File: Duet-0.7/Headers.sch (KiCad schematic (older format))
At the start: 12 parts, among them J1 EXPANSION, J10 E0 MOT/STOP, J11 E0 HEAT/TEMP/FAN, J20 5V_PS, J23 POWER IN, J24 GND V_IN, J28 Probe, J4 BED HEATER, J5 BED TEMP, J7 Z MOT/STOP, J8 Y MOT/STOP, J9 X MOT/STOP

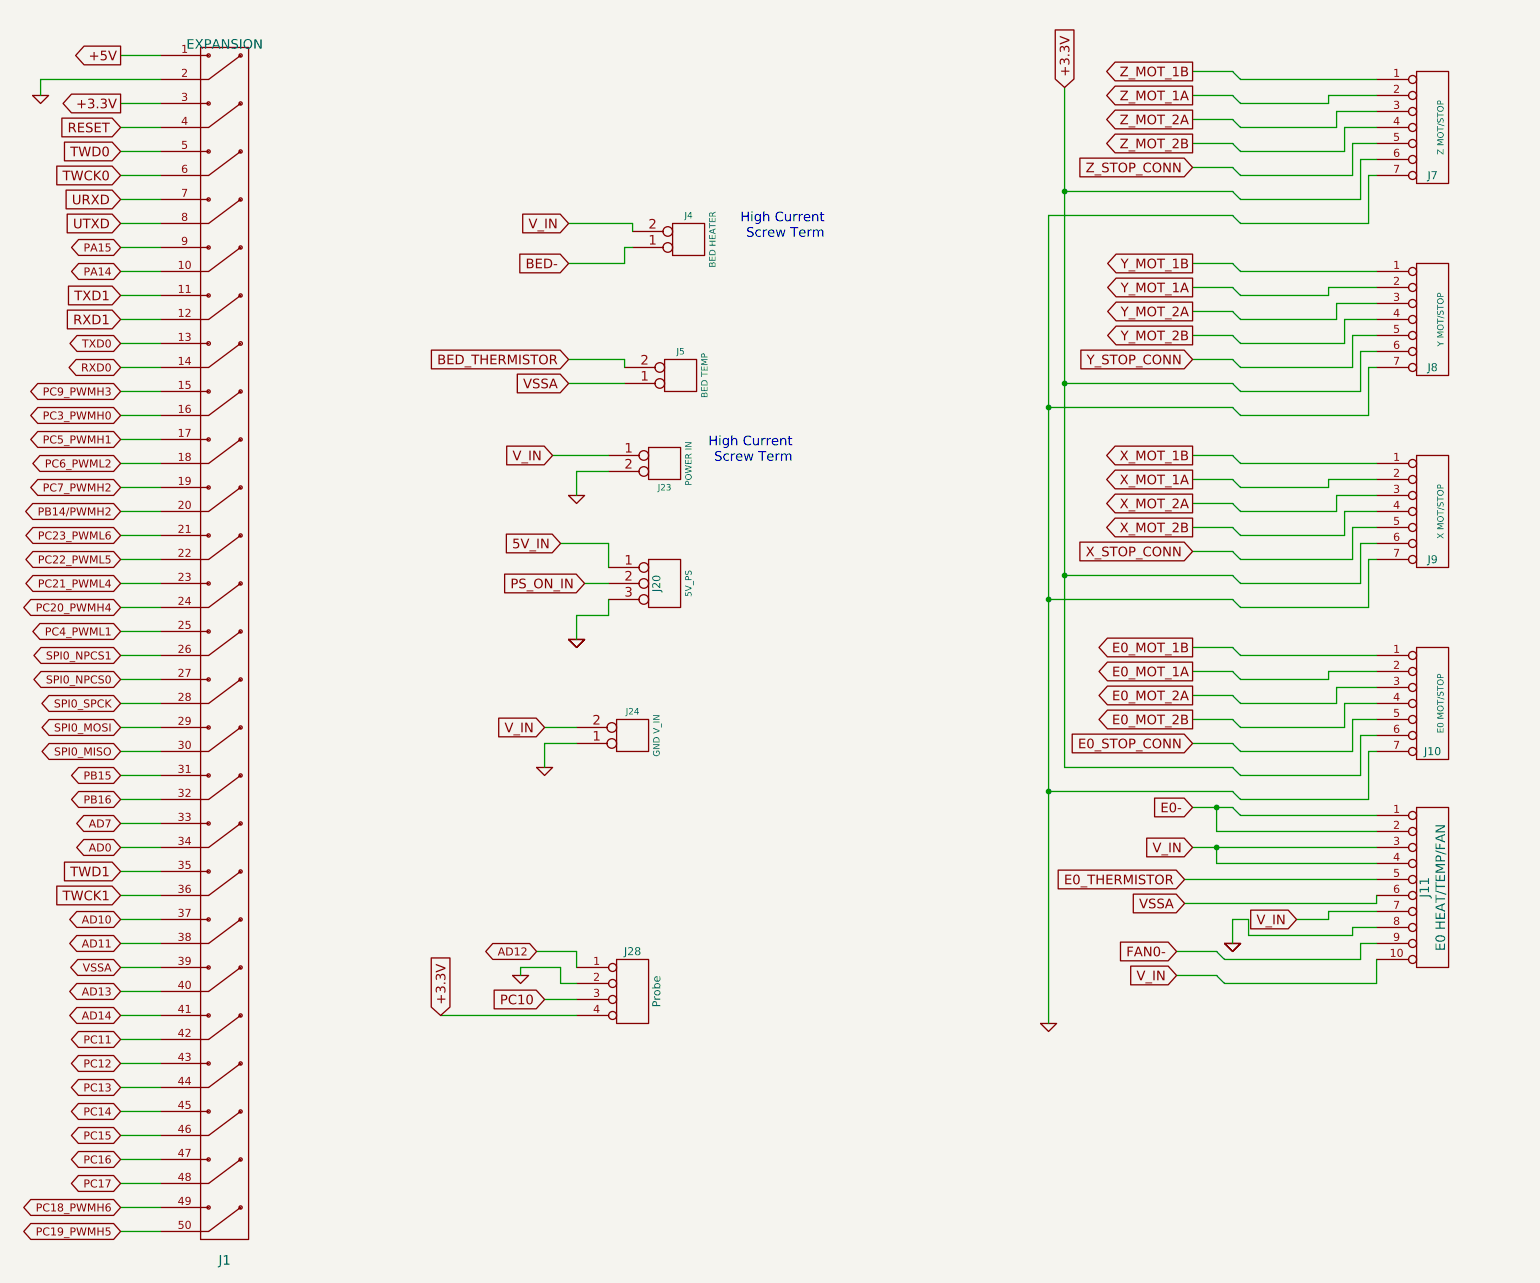
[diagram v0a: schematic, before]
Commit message: New version of Duet 0.7 - Duet 0.7a with ground plane, no chokes, and stepper and heater pin headers in the same places as on the Duet 0.6.
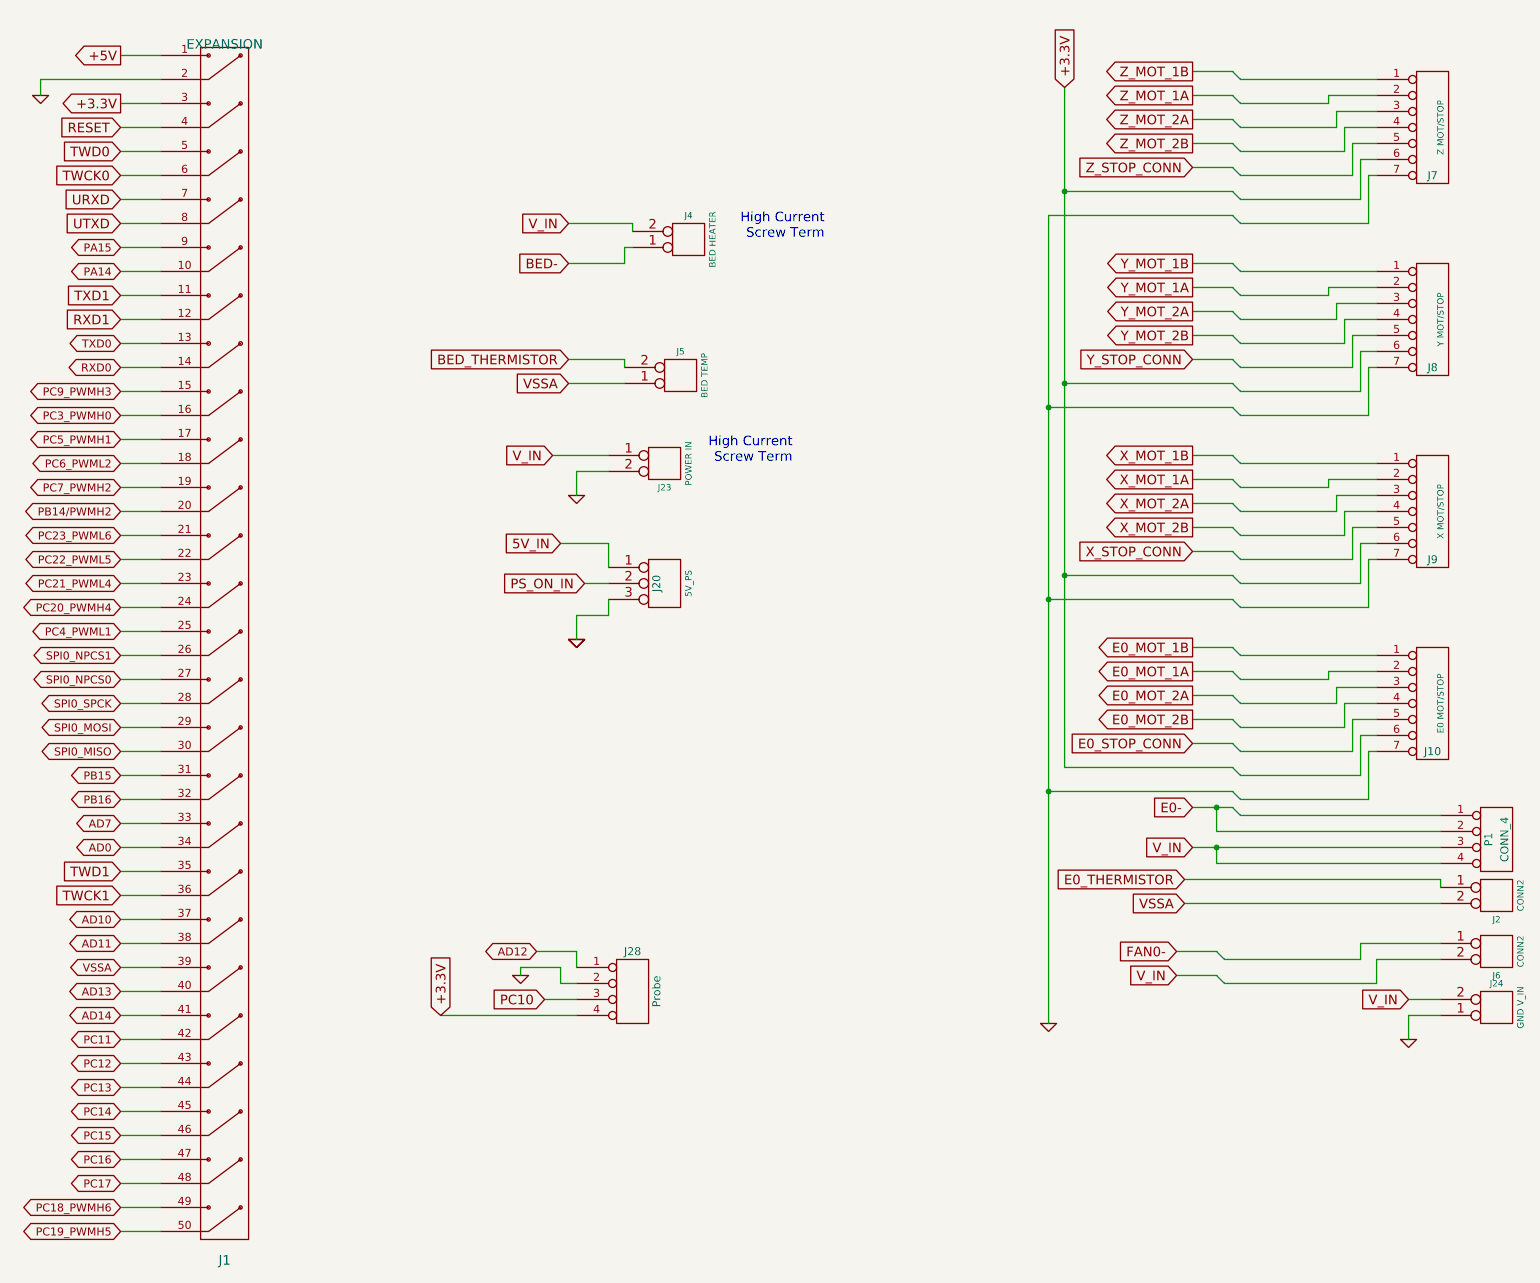
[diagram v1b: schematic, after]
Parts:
- removed J11: E0 HEAT/TEMP/FAN, symbol CONN_10
- added J2, J6: CONN2, symbol CONN2
- added P1: CONN_4, symbol CONN_4
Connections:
- net E0-: now also P1.1 (P1), P1.2 (P2)
- net E0_THERMISTOR: now also J2.1 (P1)
- net FAN0-: now also J6.1 (P1)
- net VSSA: now also J2.2 (PM)
- net V_IN: now also J6.2 (PM), P1.3 (P3), P1.4 (P4)
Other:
- moved on the sheet: J24
